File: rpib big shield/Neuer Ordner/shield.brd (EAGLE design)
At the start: 100 x 100 mm, 42 parts, among them IC1 DS2482-100S, IC2 AT24C, IC3 SAMD21G18A-AUT, IC4 DS18B20, IC5 LT1615, U1 DS1307ZN+, X1 MSTBA4

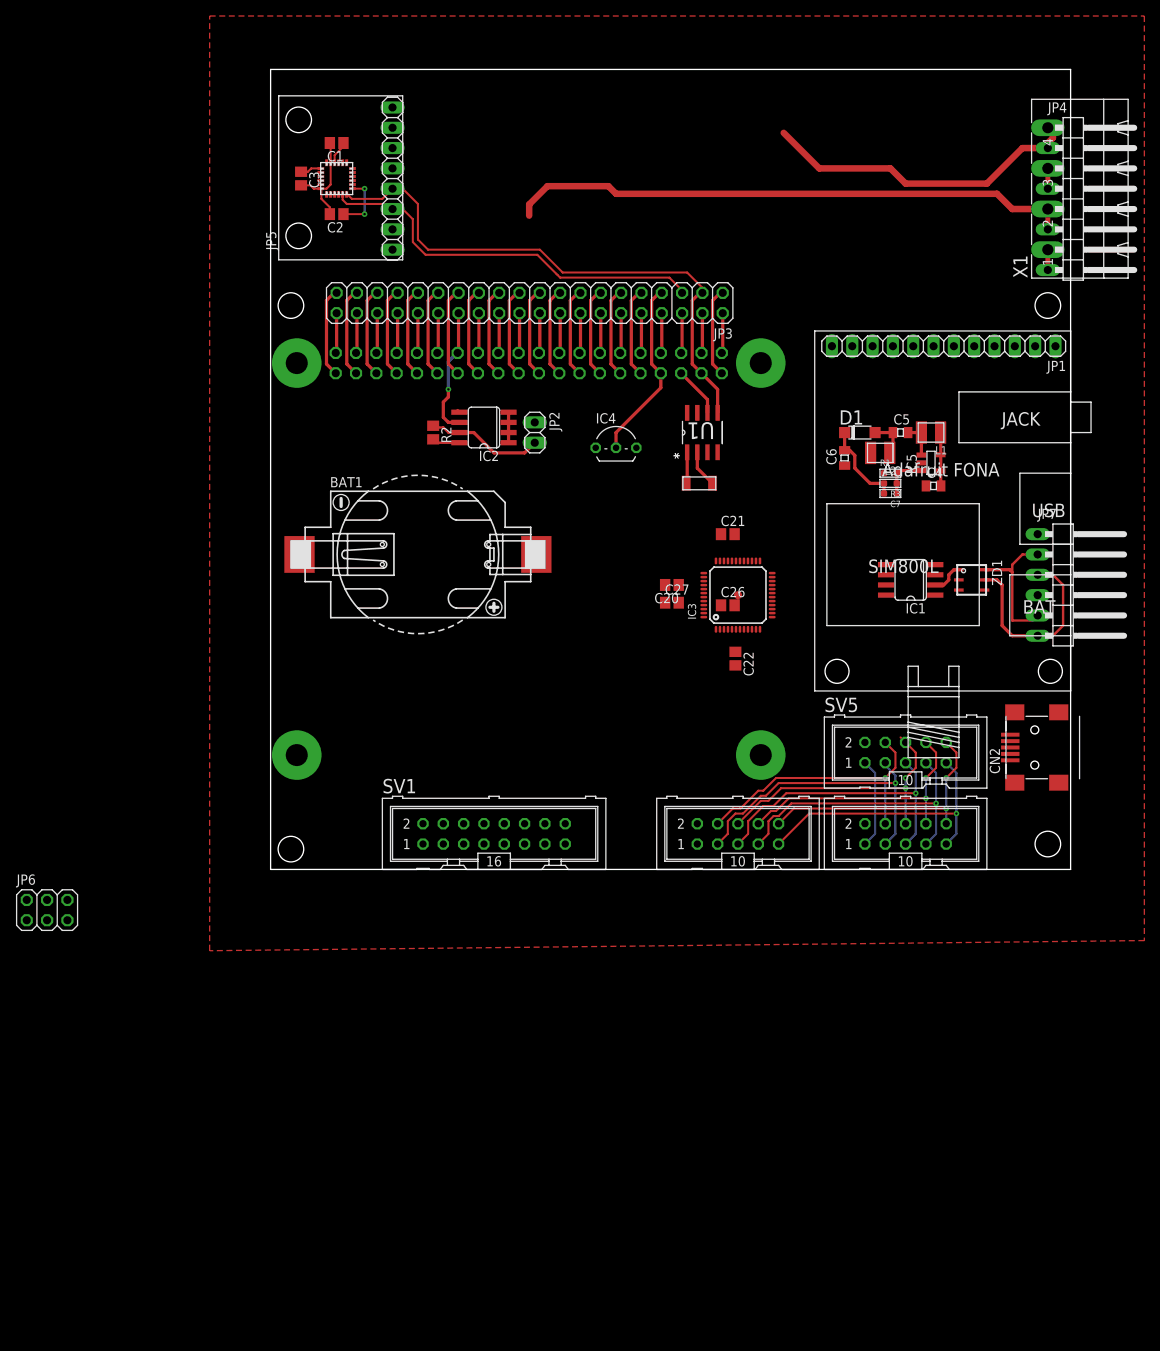
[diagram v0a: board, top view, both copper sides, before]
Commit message: lipo charger and Sepic
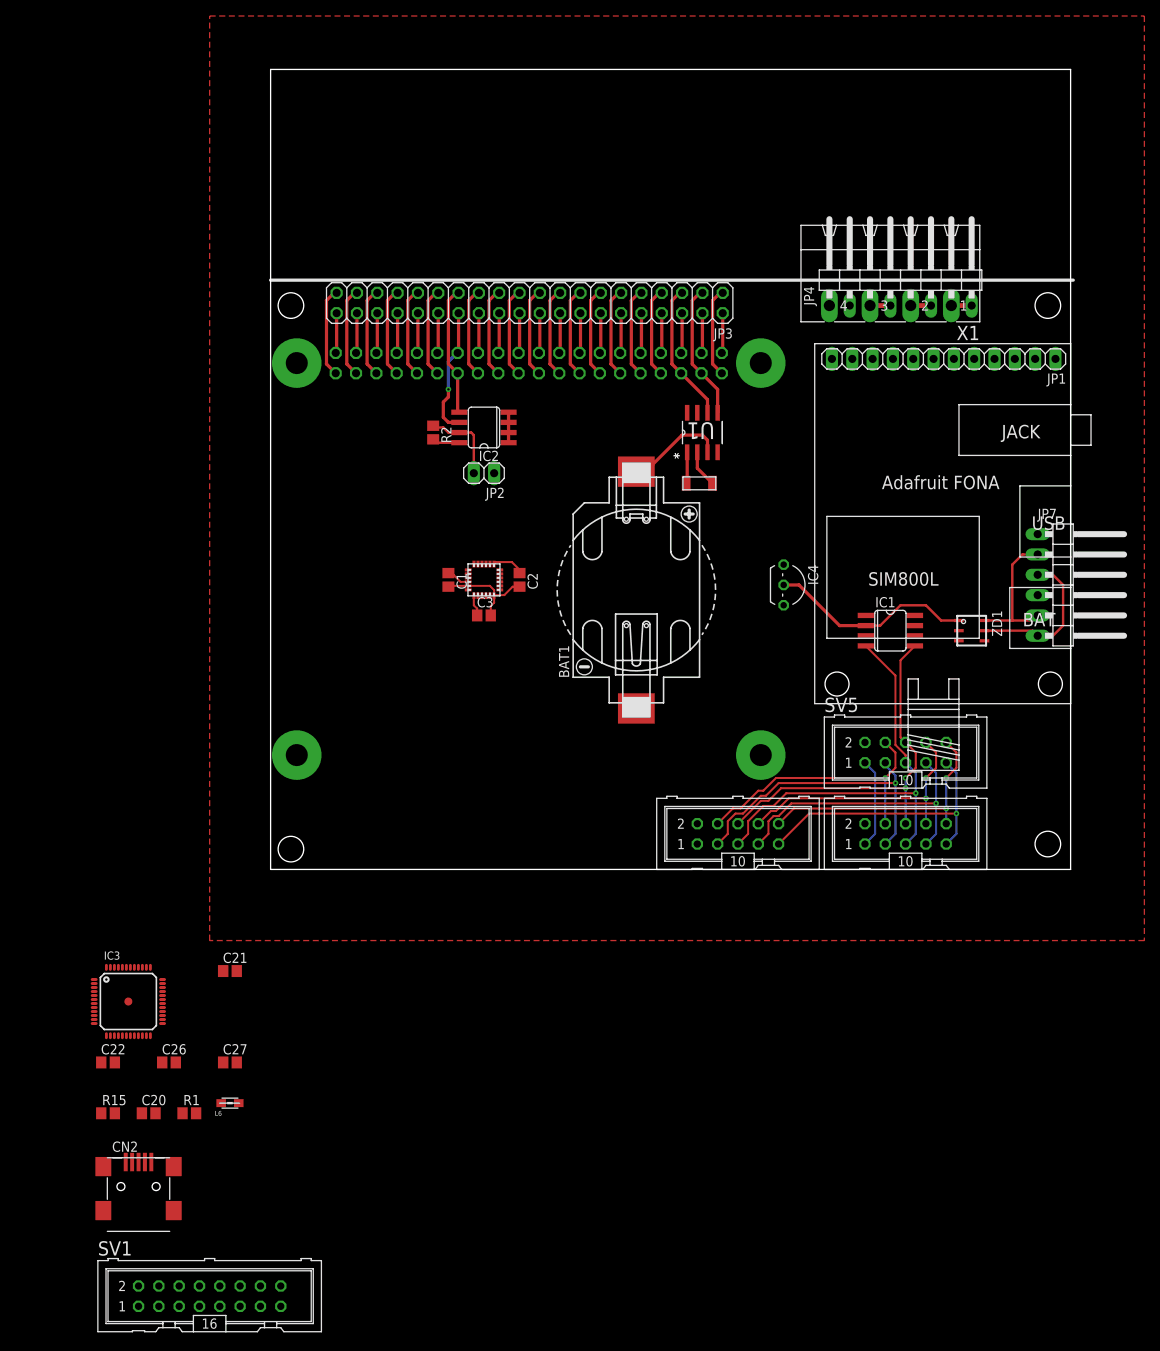
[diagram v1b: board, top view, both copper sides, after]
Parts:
- removed C4: 4µ7 10V, MYPASS:0805
- removed C5: 1µ, MYPASS:0805
- removed C6: 10µ 5V, MYPASS:0805
- removed C7: 4p7, mypassive-bleifrei:0603REFLOW
- removed D1: MBR0520L, MYDISCR:SOD123
- removed IC5: LT1615, MYLT:SOT23-5
- removed JP5: (no value), schlager_modules:GY-521
- removed JP6: (no value), pinhead:2X03
- removed L1, L2: 744032100, myinductiv:WE-LQ
- removed R3: 1M, mypassive-bleifrei:0603REFLOW
- added L6: MH2029-300Y, Protezione:0805
- added R15: 10k, schlager_passiv:R0805
- R1: value 604K -> 10k; device mypassive-bleifrei:0603REFLOW -> schlager_passiv:R0805
- moved CN2 126.1 mm to (-16.5, -40.6), turned to 0 degrees
- moved R1 118.7 mm to (-10.2, -30.5)
- moved C22 93.3 mm to (-20.3, -24.1), turned to 0 degrees
- moved C20 92.9 mm to (-15.2, -30.5), turned to 0 degrees
- moved IC3 91.6 mm to (-17.8, -16.5), turned to 0 degrees
- moved C26 90.3 mm to (-12.7, -24.1)
- moved C21 82.8 mm to (-5.08, -12.7)
- moved C27 79.7 mm to (-5.08, -24.1)
- moved SV1 67.8 mm to (-7.62, -53.3)
- moved C3 59.2 mm to (26.7, 31.8), turned to 0 degrees
- moved C1 56.4 mm to (22.2, 36.2), turned to 270 degrees
- moved U$2 53.4 mm to (26.7, 36.2), turned to 270 degrees
- moved C2 51.1 mm to (31.1, 36.2), turned to 270 degrees
- moved BAT1 27.7 mm to (45.7, 34.9), turned to 90 degrees
- moved IC4 27.1 mm to (64.1, 35.6), turned to 270 degrees
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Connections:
- net ID_SCL renamed ID_SC
- net ID_SDA renamed ID_SD
- net RPI_MISO renamed MISO
- net RPI_MOSI renamed MOSI
- net RPI_SCK renamed SCK
- removed net 12V: JP4.7, JP4.8, X1.1
- removed net ASDFASDASD: JP4.3, JP4.4, X1.3
- removed net FONA_RESET: JP1.5
- removed net FONA_RX: JP1.10
- removed net FONA_TX: JP1.9
- removed net GND_KFZ: JP4.1, JP4.2, X1.4
- removed net N$10: IC1.2, ZD1.1
- removed net N$16: C7.1, IC5.3, R1.2, R3.1
- removed net N$7: C5.2, IC5.1, L1.P$2
- removed net N$8: C5.1, D1.A, L2.P$1
- removed net N$9: C6.2, C7.2, D1.K, JP6.3, R3.2
- removed net PBAT: C4.2, IC5.4, IC5.5, JP1.1, L1.P$1
- removed net RPI_1WIRE: IC4.2, JP3.7, PCB1.7
- removed net RPI_SCL: IC1.4, JP3.5, JP5.3, PCB1.5, SV2.5, SV3.5, SV5.5, U$2.23, U1.6
- removed net RPI_SDA: IC1.5, JP3.3, JP5.4, PCB1.3, SV2.6, SV3.6, SV5.6, U$2.24, U1.5
- removed net ZUEND_KFZ: JP4.5, JP4.6, X1.2
- new net 1WIRE_DATA: IC1.2, IC4.2, JP3.7, PCB1.7, ZD1.1
- new net CS_MCP: IC3.27
- new net DGI_GPIO0: IC3.22
- new net DGI_GPIO1: IC3.30
- new net DGI_GPIO2: IC3.11
- new net N$15: C22.1, IC3.6, L6.1
- new net PA00_XIN32: IC3.1
- new net PA01_XOUT32: IC3.2
- new net PA03_AREFA: IC3.4
- new net PA08_TCC0-W0: IC3.13
- new net PA10_TCC0-W2: IC3.15
- new net PA11_TCC0-W3: IC3.16
- new net PA20_TCC0-W6: IC3.29
- new net PA27_TX_LED: IC3.39
- new net PA28_USB_HOST_EN: IC3.41
- new net PB02_AIN10: IC3.47
- new net PB03_RX_LED: IC3.48
- new net PB10_S4_SPI_MOSI: IC3.19
- new net PB11_S4_SPI_SCK: IC3.20
- new net PB12_S4_SPI_MISO: IC3.21
- new net SCL: IC1.4, IC3.32, JP3.5, PCB1.5, R1.1, SV2.5, SV3.5, SV5.5, U$2.23, U1.6
- new net SDA: IC1.5, IC3.31, JP3.3, PCB1.3, R15.1, SV2.6, SV3.6, SV5.6, U$2.24, U1.5
- net +3V3: now also L6.2, R1.2, R15.2; no longer C22.1, IC3.6, JP6.2, JP6.4
- net GND: now also JP4.1, JP4.2, X1.4; no longer C4.1, C6.1, IC5.2, JP1.2, JP1.7, JP5.2, L2.P$2, R1.1, U$2.9
- net HALTE_RELAI: now also JP4.5, JP4.6, X1.2
- net P3V3: no longer JP5.1, JP6.1
- net P5V: now also JP4.7, JP4.8, X1.1
- net ZUENDPLUS_LED2: now also JP4.3, JP4.4, X1.3
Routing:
- net RPI_SDA: track 105.5 -> 0.00 mm, vias 2 -> 0
- net RPI_SCL: track 93.1 -> 0.00 mm, vias 1 -> 0
- net SCL: track 0.00 -> 71.2 mm, vias 0 -> 1
- net ZUEND_KFZ: track 70.9 -> 0.00 mm
- net SDA: track 0.00 -> 64.1 mm, vias 0 -> 2
- net GND_KFZ: track 41.8 -> 0.00 mm
- net 1WIRE_DATA: track 0.00 -> 37.1 mm
- net RPI_1WIRE: track 22.9 -> 0.00 mm
- net N$1: track 0.00 -> 12.6 mm
- net N$9: track 11.1 -> 0.00 mm
- net PBAT: track 6.69 -> 0.00 mm
- net N$16: track 5.74 -> 0.00 mm
- net N$2: track 25.0 -> 19.4 mm
- net N$8: track 4.95 -> 0.00 mm
- net ID_SD: track 11.5 -> 16.2 mm
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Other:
- board text added: "ENC/LED"
